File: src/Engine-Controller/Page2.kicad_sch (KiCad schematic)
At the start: 30 parts, among them P10 282837-2, P2 282837-6, P4 Micro_SD_Card, P5 USB, P6 140-504-415-000, P9 5015680807, Q1 QS5U17TR, U11 TS391IYLT, U4 SST25VF040B-50-4I-S2AE-T, U5 CP2102-GMR(QFN28)

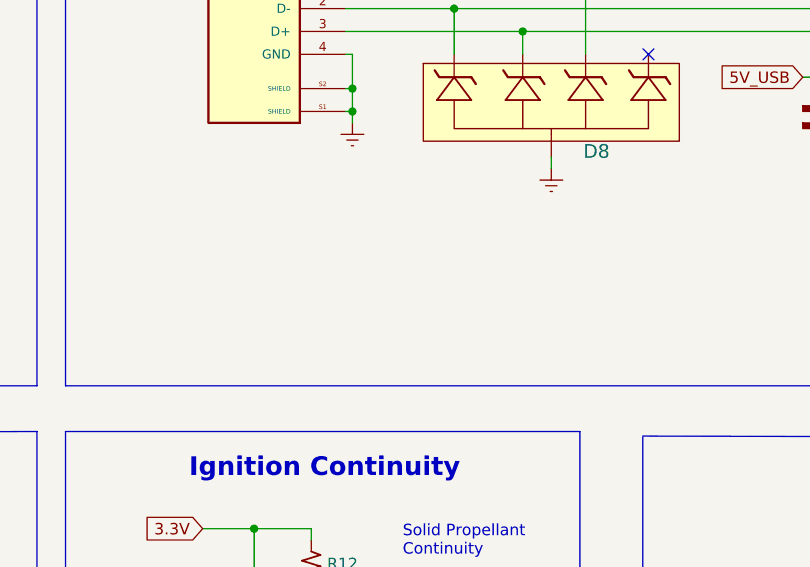
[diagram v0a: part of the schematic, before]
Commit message: created rev5 schematic, added USB detection, updated PT readout circuits
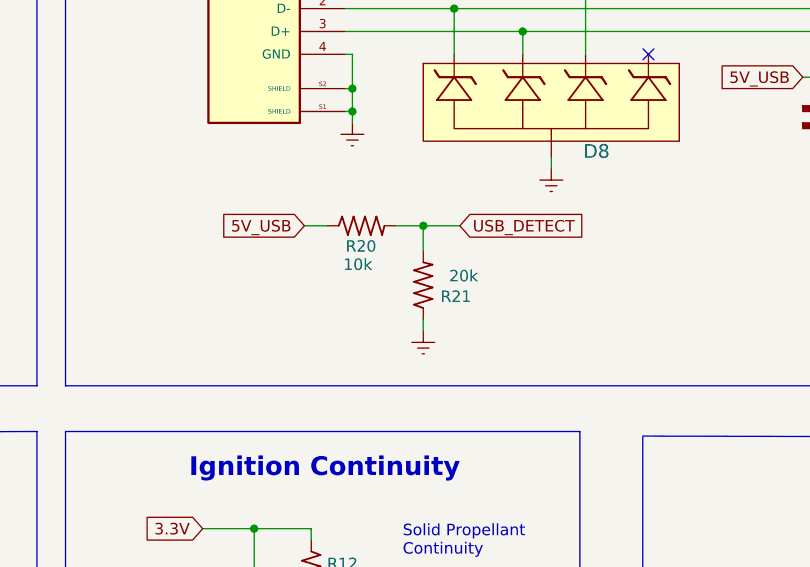
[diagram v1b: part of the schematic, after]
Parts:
- added R20: 10k, Engine-Controller:RES_0603, symbol Engine-Controller:RES_0603
- added R21: 20k, Engine-Controller:RES_0603, symbol Engine-Controller:RES_0603
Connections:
- net 5V_USB: now also R20.1
- net Earth: now also R21.1
- new net USB_DETECT: R20.2, R21.2

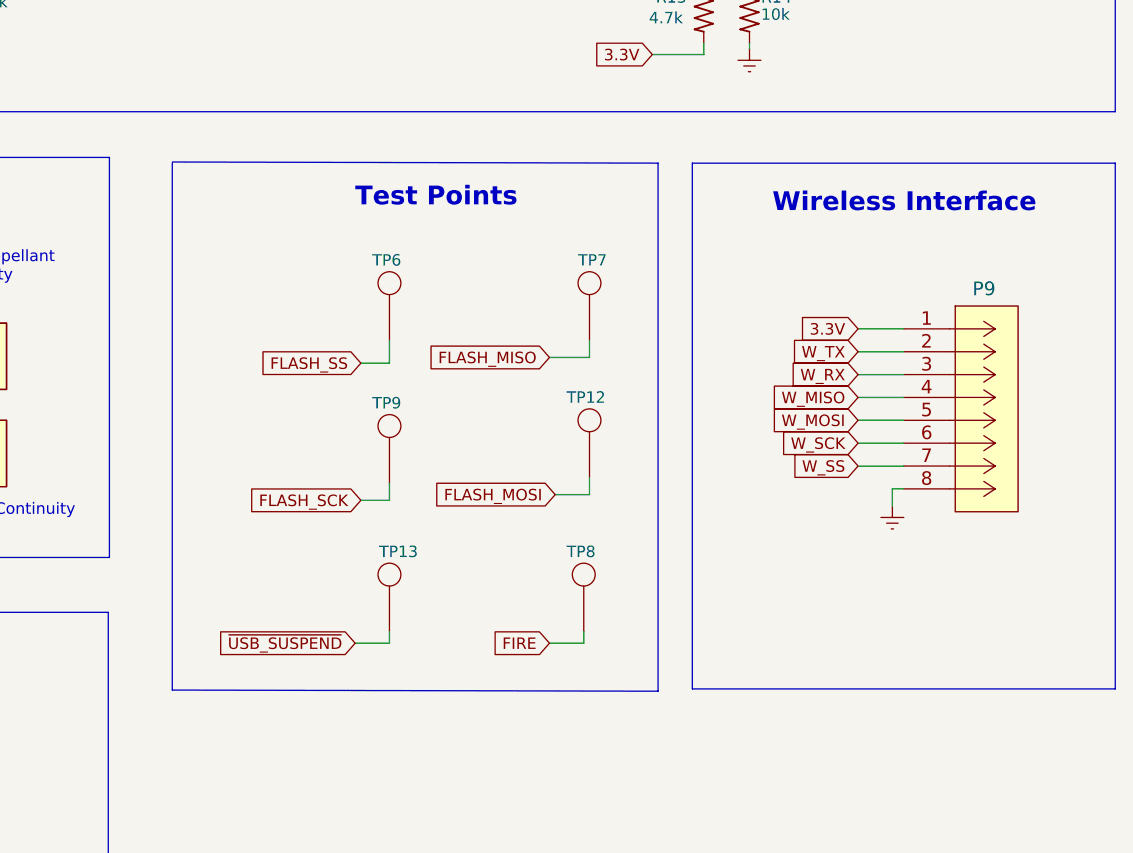
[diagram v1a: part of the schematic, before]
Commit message: removed wireless interface connector
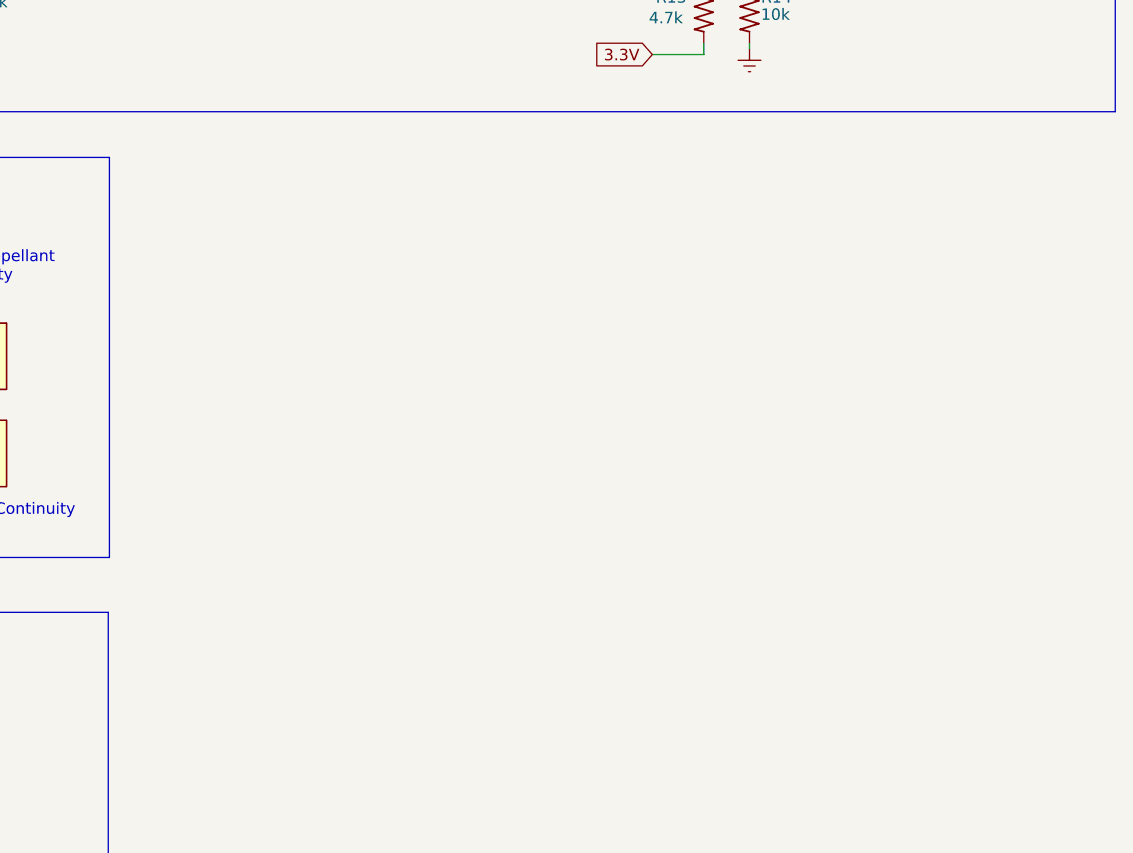
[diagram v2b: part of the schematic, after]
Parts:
- removed P9: 5015680807, Engine-Controller:5015680807, symbol Engine-Controller:5015680807
- removed TP12, TP13, TP6, TP7, TP8, TP9: TP, Engine-Controller:TP, symbol Engine-Controller:TP
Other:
- note removed: "Test Points"
- note removed: "Wireless Interface"

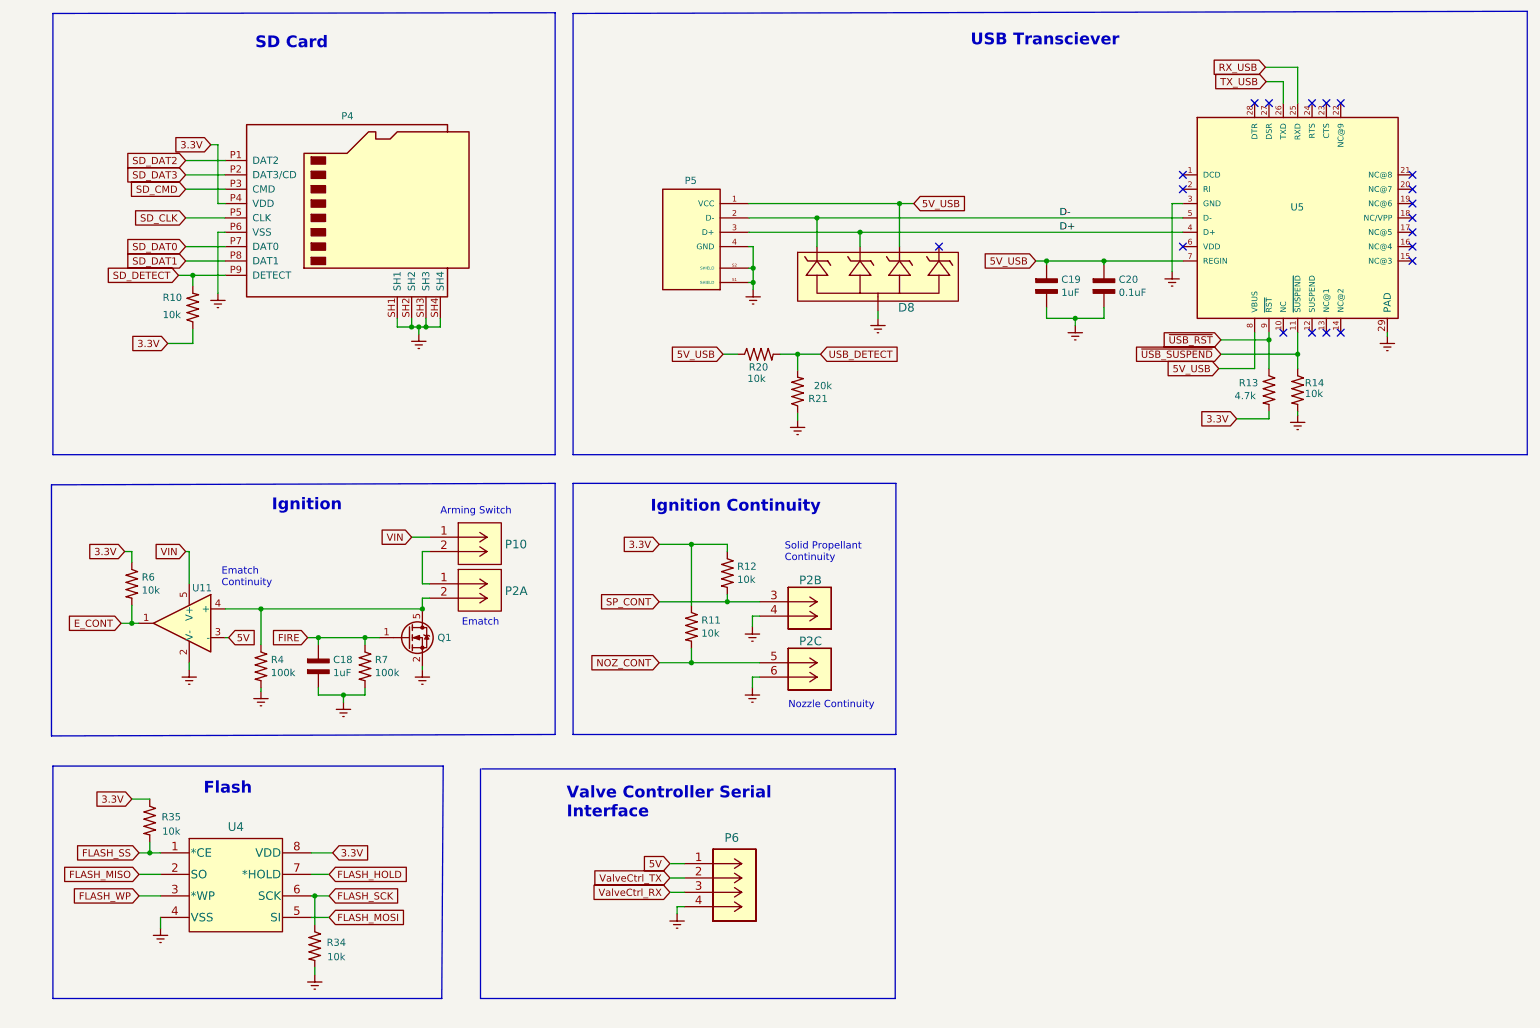
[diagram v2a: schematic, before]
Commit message: implemented RS485 interface
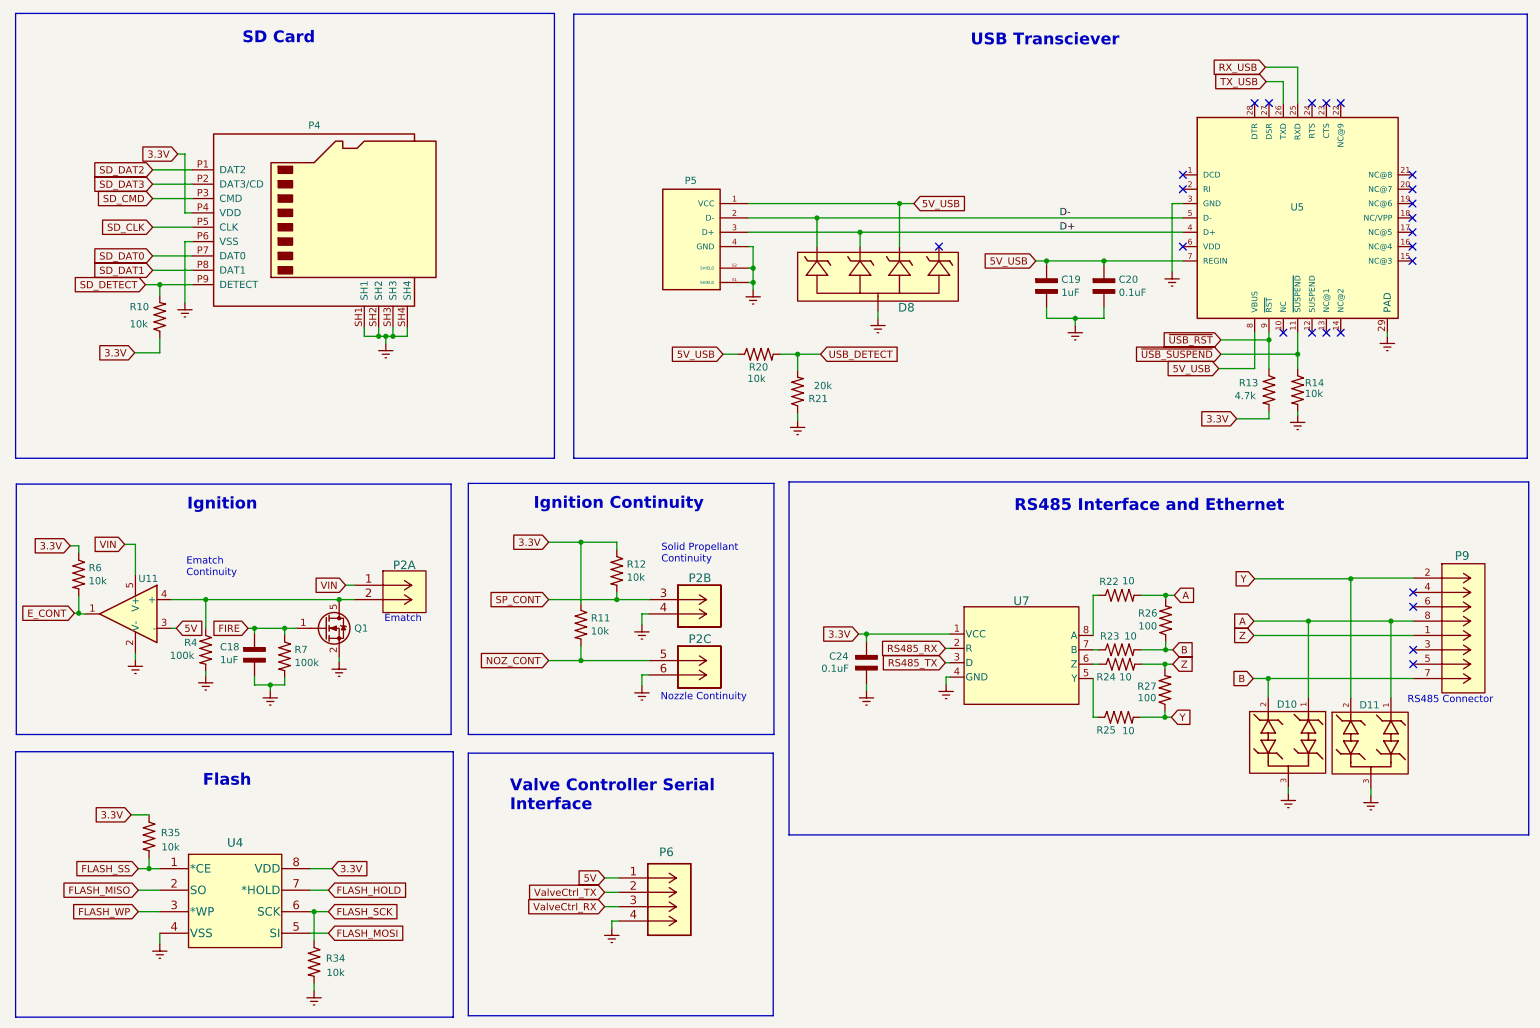
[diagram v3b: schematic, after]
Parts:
- removed P10: 282837-2, Engine-Controller:282837-2, symbol Engine-Controller:282837-2
- added C24: 0.1uF, Engine-Controller:CAP_0603, symbol Engine-Controller:CAP_0603
- added D10, D11: SMBJ36CA-13-F, Engine-Controller:CDSOT23-SM712, symbol Engine-Controller:CDSOT23-SM712
- added P9: 54602-908LF, Engine-Controller:54602-908LF, symbol Engine-Controller:54602-908LF
- added R22, R23, R24, R25: 10, symbol Engine-Controller:RES_0603
- added R26, R27: 100, symbol Engine-Controller:RES_0603
- added U7: SN65HVD71DR, Engine-Controller:SN65HVD71DR, symbol Engine-Controller:SN65HVD71DR
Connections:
- net 3.3V: now also C24.2, U7.1 (VCC)
- net Earth: now also C24.1, D10.3, D11.3, U7.4 (GND)
- net VIN: now also P2.1 (5)
- new net: R25.1, U7.5 (Y)
- new net: R24.1, U7.6 (Z)
- new net: R23.1, U7.7 (B)
- new net: R22.1, U7.8 (A)
- new net A: D10.1, D11.1, P9.8, R22.2, R26.2
- new net B: D10.2, P9.7, R23.2, R26.1
- new net RS485_RX: U7.2 (R)
- new net RS485_TX: U7.3 (D)
- new net Y: D11.2, P9.2, R25.2, R27.1
- new net Z: P9.1, R24.2, R27.2
- no-connect marks 20 -> 24
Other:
- note added: "RS485 Connector"
- note added: "RS485 Interface and Ethernet"
- note removed: "Arming Switch"
- moved on the sheet: C18, P2A, P2B, P2C, P4, P6, Q1, R10, R11, R12, R34, R35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

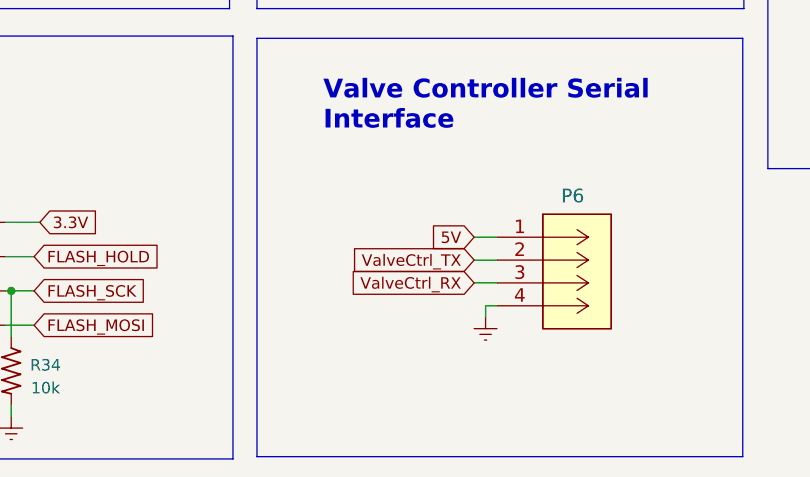
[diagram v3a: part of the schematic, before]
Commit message: fixed valve controller connector by reversing connections
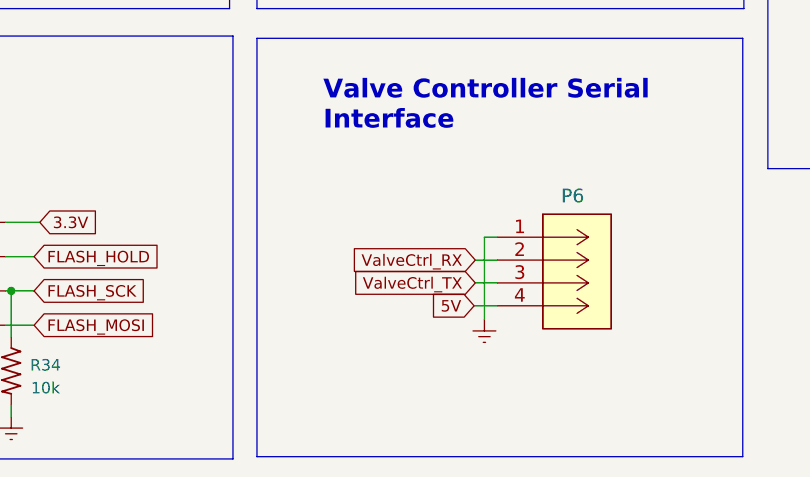
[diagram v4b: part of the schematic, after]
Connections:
- net 5V: now also P6.4; no longer P6.1 (+12V)
- net Earth: now also P6.1 (+12V); no longer P6.4
- net ValveCtrl_RX: now also P6.2 (GND); no longer P6.3
- net ValveCtrl_TX: now also P6.3; no longer P6.2 (GND)
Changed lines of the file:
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@@
+    (stroke (width 0) (type default))
+  )
+  (wire (pts (xy 118.11 176.53) (xy 120.523 176.53))
     (stroke (width 0) (type default))
   )
@@
     (stroke (width 0) (type default))
   )
-  (wire (pts (xy 117.983 176.53) (xy 120.523 176.53))
-    (stroke (width 0) (type default))
-  )
   (wire (pts (xy 56.007 137.287) (xy 58.801 137.287))
     (stroke (width 0) (type default))
@@
     (stroke (width 0) (type default))
   )
+  (wire (pts (xy 118.11 173.99) (xy 120.523 173.99))
+    (stroke (width 0) (type default))
+  )
   (wire (pts (xy 113.792 112.014) (xy 108.077 112.014))
     (stroke (width 0) (type default))
@@
     (stroke (width 0) (type default))
   )
-  (wire (pts (xy 117.983 171.45) (xy 120.523 171.45))
-    (stroke (width 0) (type default))
-  )
-  (wire (pts (xy 119.253 179.07) (xy 119.253 180.34))
-    (stroke (width 0) (type default))
-  )
   (wire (pts (xy 166.37 71.12) (xy 166.37 72.39))
     (stroke (width 0) (type default))
@@
     (stroke (width 0) (type default))
   )
-  (wire (pts (xy 120.523 179.07) (xy 119.253 179.07))
-    (stroke (width 0) (type default))
-  )
   (wire (pts (xy 77.978 74.041) (xy 77.978 75.565))
     (stroke (width 0) (type default))
@@
     (stroke (width 0) (type default))
   )
+  (wire (pts (xy 117.983 179.07) (xy 120.523 179.07))
+    (stroke (width 0) (type default))
+  )
   (wire (pts (xy 113.792 132.969) (xy 113.792 130.429))
     (stroke (width 0) (type default))
@@
     (stroke (width 0) (type default))
   )
+  (wire (pts (xy 119.126 171.45) (xy 119.126 180.594))
+    (stroke (width 0) (type default))
+  )
   (wire (pts (xy 39.243 66.421) (xy 44.958 66.421))
     (stroke (width 0) (type default))
@@
     (stroke (width 0) (type default))
   )
-  (wire (pts (xy 117.983 173.99) (xy 120.523 173.99))
-    (stroke (width 0) (type default))
-  )
   (wire (pts (xy 35.433 173.609) (xy 39.243 173.609))
     (stroke (width 0) (type default))
@@
   )
   (wire (pts (xy 238.125 34.29) (xy 238.125 30.48))
+    (stroke (width 0) (type default))
+  )
+  (wire (pts (xy 120.523 171.45) (xy 119.126 171.45))
     (stroke (width 0) (type default))
   )
@@
     )
   )
-  (global_label "5V" (shape input) (at 117.983 171.45 180) (fields_autoplaced)
-    (effects (font (size 1.27 1.27)) (justify right))
-    (property "Intersheetrefs" "${INTERSHEET_REFS}" (at 113.3607 171.3706 0)
-      (effects (font (size 1.27 1.27)) (justify right) hide)
-    )
-  )
-  (global_label "ValveCtrl_TX" (shape input) (at 117.983 173.99 180) (fields_autoplaced)
-    (effects (font (size 1.27 1.27)) (justify right))
-    (property "Intersheetrefs" "${INTERSHEET_REFS}" (at 104.1078 173.9106 0)
+  (global_label "5V" (shape input) (at 117.983 179.07 180) (fields_autoplaced)
+    (effects (font (size 1.27 1.27)) (justify right))
+    (property "Intersheetrefs" "${INTERSHEET_REFS}" (at 113.3607 178.9906 0)
+      (effects (font (size 1.27 1.27)) (justify right) hide)
+    )
+  )
+  (global_label "ValveCtrl_TX" (shape input) (at 118.11 176.53 180) (fields_autoplaced)
+    (effects (font (size 1.27 1.27)) (justify right))
+    (property "Intersheetrefs" "${INTERSHEET_REFS}" (at 104.2348 176.4506 0)
       (effects (font (size 1.27 1.27)) (justify right) hide)
     )
@@
     )
   )
-  (global_label "ValveCtrl_RX" (shape input) (at 117.983 176.53 180) (fields_autoplaced)
-    (effects (font (size 1.27 1.27)) (justify right))
-    (property "Intersheetrefs" "${INTERSHEET_REFS}" (at 103.8055 176.4506 0)
+  (global_label "ValveCtrl_RX" (shape input) (at 118.11 173.99 180) (fields_autoplaced)
+    (effects (font (size 1.27 1.27)) (justify right))
+    (property "Intersheetrefs" "${INTERSHEET_REFS}" (at 103.9325 173.9106 0)
       (effects (font (size 1.27 1.27)) (justify right) hide)
     )
@@
     )
   )
-  (symbol (lib_name "Earth_1") (lib_id "Engine-Controller:Earth") (at 119.253 180.34 0) (unit 1)
+  (symbol (lib_name "Earth_1") (lib_id "Engine-Controller:Earth") (at 119.126 180.594 0) (unit 1)
     (in_bom yes) (on_board yes) (dnp no) (fields_autoplaced)
-    (property "Reference" "#PWR028" (at 119.253 186.69 0)
-      (effects (font (size 1.27 1.27)) hide)
-    )
-    (property "Value" "Earth" (at 119.253 184.15 0)
-      (effects (font (size 1.27 1.27)) hide)
-    )
-    (property "Footprint" "" (at 119.253 180.34 0)
-      (effects (font (size 1.27 1.27)) hide)
-    )
-    (property "Datasheet" "" (at 119.253 180.34 0)
-      (effects (font (size 1.27 1.27)) hide)
-    )
+    (property "Reference" "#PWR028" (at 119.126 186.944 0)
+      (effects (font (size 1.27 1.27)) hide)
+    )
+    (property "Value" "Earth" (at 119.126 184.404 0)
+      (effects (font (size 1.27 1.27)) hide)
+    )
+    (property "Footprint" "" (at 119.126 180.594 0)
+      (effects (font (size 1.27 1.27)) hide)
+    )
+    (property "Datasheet" "" (at 119.126 180.594 0)
+      (effects (font (size 1.27 1.27)) hide)
+    )
